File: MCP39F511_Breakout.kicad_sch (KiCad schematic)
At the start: 27 parts, among them J1 Conn_01x10, U1 MCP39F511-E_MQ, U2 MCP9700T-ETT, Y1 4MHz / 16pF

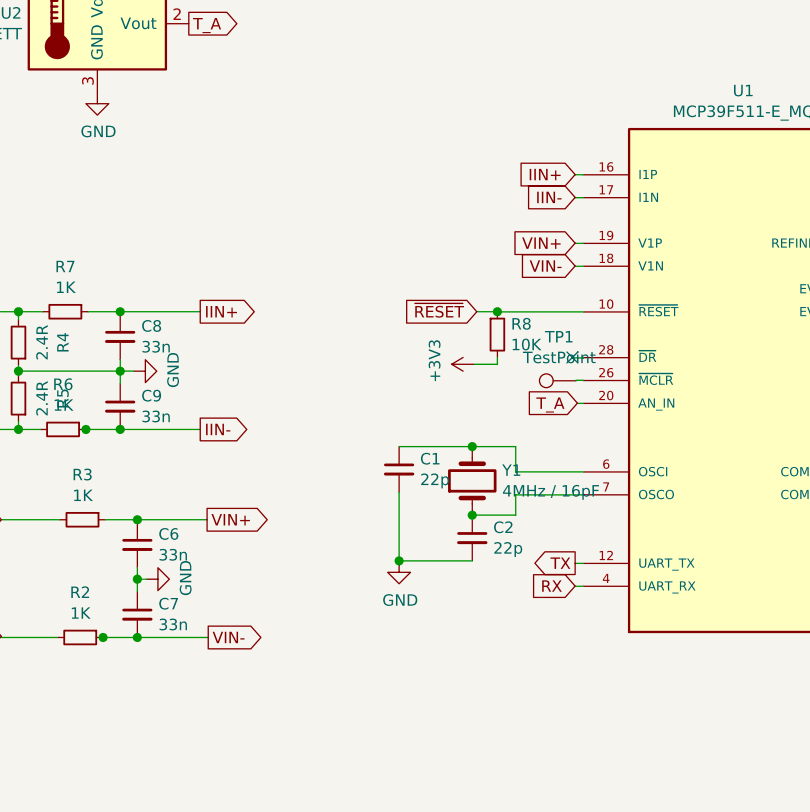
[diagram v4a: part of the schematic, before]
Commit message: Add MCLR pullup
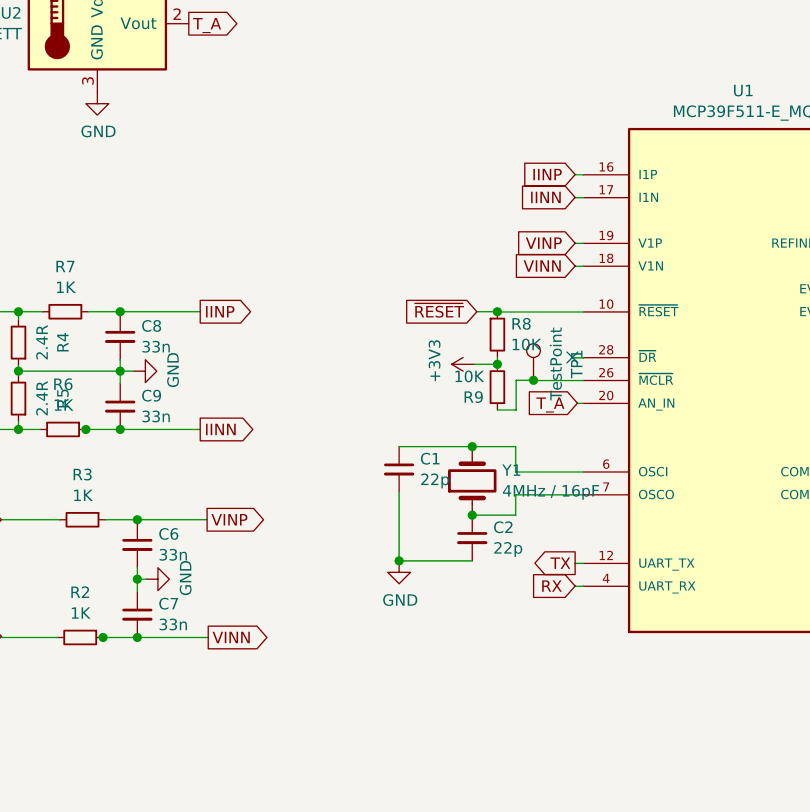
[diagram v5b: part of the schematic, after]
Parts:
- added R9: 10K, Resistor_SMD:R_0603_1608Metric, symbol Device:R_Small
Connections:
- net +3V3: now also R9.2
- net at TP1.1, U1.26 (~MCLR): now also R9.1
- net IIN+ renamed IINP
- net IIN- renamed IINN
- net VIN+ renamed VINP
- net VIN- renamed VINN
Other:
- moved on the sheet: TP1
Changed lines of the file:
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@@
   (junction (at 103.886 98.044) (diameter 1.016) (color 0 0 0 0))
   (junction (at 106.68 75.438) (diameter 1.016) (color 0 0 0 0))
+  (junction (at 106.68 81.28) (diameter 1.016) (color 0 0 0 0))
+  (junction (at 110.6932 83.058) (diameter 1.016) (color 0 0 0 0))
   (junction (at 151.7904 105.9434) (diameter 1.016) (color 0 0 0 0))
   (junction (at 151.7904 108.458) (diameter 1.016) (color 0 0 0 0))
@@
     (stroke (width 0) (type solid) (color 0 0 0 0))
   )
+  (wire (pts (xy 108.7628 83.058) (xy 108.7628 86.36))
+    (stroke (width 0) (type solid) (color 0 0 0 0))
+  )
+  (wire (pts (xy 108.7628 86.36) (xy 106.68 86.36))
+    (stroke (width 0) (type solid) (color 0 0 0 0))
+  )
+  (wire (pts (xy 110.6932 83.058) (xy 108.7628 83.058))
+    (stroke (width 0) (type solid) (color 0 0 0 0))
+  )
+  (wire (pts (xy 110.6932 83.0834) (xy 110.6932 83.058))
+    (stroke (width 0) (type solid) (color 0 0 0 0))
+  )
   (wire (pts (xy 115.0112 80.518) (xy 115.0112 80.5688))
     (stroke (width 0) (type solid) (color 0 0 0 0))
@@
     (stroke (width 0) (type solid) (color 0 0 0 0))
   )
-  (wire (pts (xy 115.4176 83.058) (xy 115.4176 83.1088))
-    (stroke (width 0) (type solid) (color 0 0 0 0))
-  )
   (wire (pts (xy 115.57 85.6234) (xy 115.57 85.598))
     (stroke (width 0) (type solid) (color 0 0 0 0))
@@
     (stroke (width 0) (type solid) (color 0 0 0 0))
   )
-  (wire (pts (xy 116.2304 83.058) (xy 115.4176 83.058))
-    (stroke (width 0) (type solid) (color 0 0 0 0))
-  )
-  (wire (pts (xy 116.2304 83.058) (xy 116.2304 83.0834))
+  (wire (pts (xy 116.2304 83.0834) (xy 110.6932 83.0834))
     (stroke (width 0) (type solid) (color 0 0 0 0))
   )
@@
     (effects (font (size 1.27 1.27)) (justify left))
   )
-  (global_label "IIN+" (shape output) (at 73.66 75.438 0)
+  (global_label "IINP" (shape output) (at 73.66 75.438 0)
     (effects (font (size 1.27 1.27)) (justify left))
   )
-  (global_label "IIN-" (shape output) (at 73.66 88.519 0)
+  (global_label "IINN" (shape output) (at 73.66 88.519 0)
     (effects (font (size 1.27 1.27)) (justify left))
   )
-  (global_label "VIN+" (shape output) (at 74.422 98.552 0)
+  (global_label "VINP" (shape output) (at 74.422 98.552 0)
     (effects (font (size 1.27 1.27)) (justify left))
   )
-  (global_label "VIN-" (shape output) (at 74.549 111.633 0)
+  (global_label "VINN" (shape output) (at 74.549 111.633 0)
     (effects (font (size 1.27 1.27)) (justify left))
   )
@@
     (effects (font (size 1.27 1.27)) (justify right))
   )
-  (global_label "IIN+" (shape input) (at 115.316 60.198 180)
+  (global_label "IINP" (shape input) (at 115.316 60.198 180)
     (effects (font (size 1.27 1.27)) (justify right))
   )
-  (global_label "IIN-" (shape input) (at 115.316 62.738 180)
+  (global_label "IINN" (shape input) (at 115.316 62.738 180)
     (effects (font (size 1.27 1.27)) (justify right))
   )
-  (global_label "VIN+" (shape input) (at 115.316 67.818 180)
+  (global_label "VINP" (shape input) (at 115.316 67.818 180)
     (effects (font (size 1.27 1.27)) (justify right))
   )
-  (global_label "VIN-" (shape input) (at 115.316 70.358 180)
+  (global_label "VINN" (shape input) (at 115.316 70.358 180)
     (effects (font (size 1.27 1.27)) (justify right))
   )
@@
     (effects (font (size 1.27 1.27)) (justify right))
   )
-  (symbol (lib_id "Connector:TestPoint") (at 115.4176 83.1088 90) (unit 1)
-    (in_bom yes) (on_board yes)
-    (property "Reference" "TP1" (id 0) (at 113.5761 78.2636 90))
-    (property "Value" "TestPoint" (id 1) (at 113.5761 80.5623 90))
-    (property "Footprint" "TestPoint:TestPoint_Pad_D2.0mm" (id 2) (at 115.4176 78.0288 0)
-      (effects (font (size 1.27 1.27)) hide)
-    )
-    (property "Datasheet" "~" (id 3) (at 115.4176 78.0288 0)
-      (effects (font (size 1.27 1.27)) hide)
-    )
-    (property "DNP" "..." (id 4) (at 115.4176 83.1088 0)
+  (symbol (lib_id "Connector:TestPoint") (at 110.6932 83.058 0) (unit 1)
+    (in_bom yes) (on_board yes)
+    (property "Reference" "TP1" (id 0) (at 115.5384 81.2165 90))
+    (property "Value" "TestPoint" (id 1) (at 113.2397 81.2165 90))
+    (property "Footprint" "TestPoint:TestPoint_Pad_D2.0mm" (id 2) (at 115.7732 83.058 0)
+      (effects (font (size 1.27 1.27)) hide)
+    )
+    (property "Datasheet" "~" (id 3) (at 115.7732 83.058 0)
+      (effects (font (size 1.27 1.27)) hide)
+    )
+    (property "DNP" "..." (id 4) (at 110.6932 83.058 0)
       (effects (font (size 1.27 1.27)) hide)
     )
@@
     )
     (property "manf#" "RC0603FR-0710KL" (id 4) (at 106.68 77.978 0)
+      (effects (font (size 1.27 1.27)) hide)
+    )
+  )
+  (symbol (lib_id "Device:R_Small") (at 106.68 83.82 180) (unit 1)
+    (in_bom yes) (on_board yes)
+    (property "Reference" "R9" (id 0) (at 105.1813 84.9694 0)
+      (effects (font (size 1.27 1.27)) (justify left))
+    )
+    (property "Value" "10K" (id 1) (at 105.1813 82.6707 0)
+      (effects (font (size 1.27 1.27)) (justify left))
+    )
+    (property "Footprint" "Resistor_SMD:R_0603_1608Metric" (id 2) (at 106.68 83.82 0)
+      (effects (font (size 1.27 1.27)) hide)
+    )
+    (property "Datasheet" "~" (id 3) (at 106.68 83.82 0)
+      (effects (font (size 1.27 1.27)) hide)
+    )
+    (property "manf#" "RC0603FR-0710KL" (id 4) (at 106.68 83.82 0)
       (effects (font (size 1.27 1.27)) hide)
     )
@@
       (reference "R8") (unit 1) (value "10K") (footprint "Resistor_SMD:R_0603_1608Metric")
     )
+    (path "/81d999fc-596b-402f-991d-76c616dcb90b"
+      (reference "R9") (unit 1) (value "10K") (footprint "Resistor_SMD:R_0603_1608Metric")
+    )
     (path "/12887168-a49a-4745-9d00-7dfb93b5e52d"

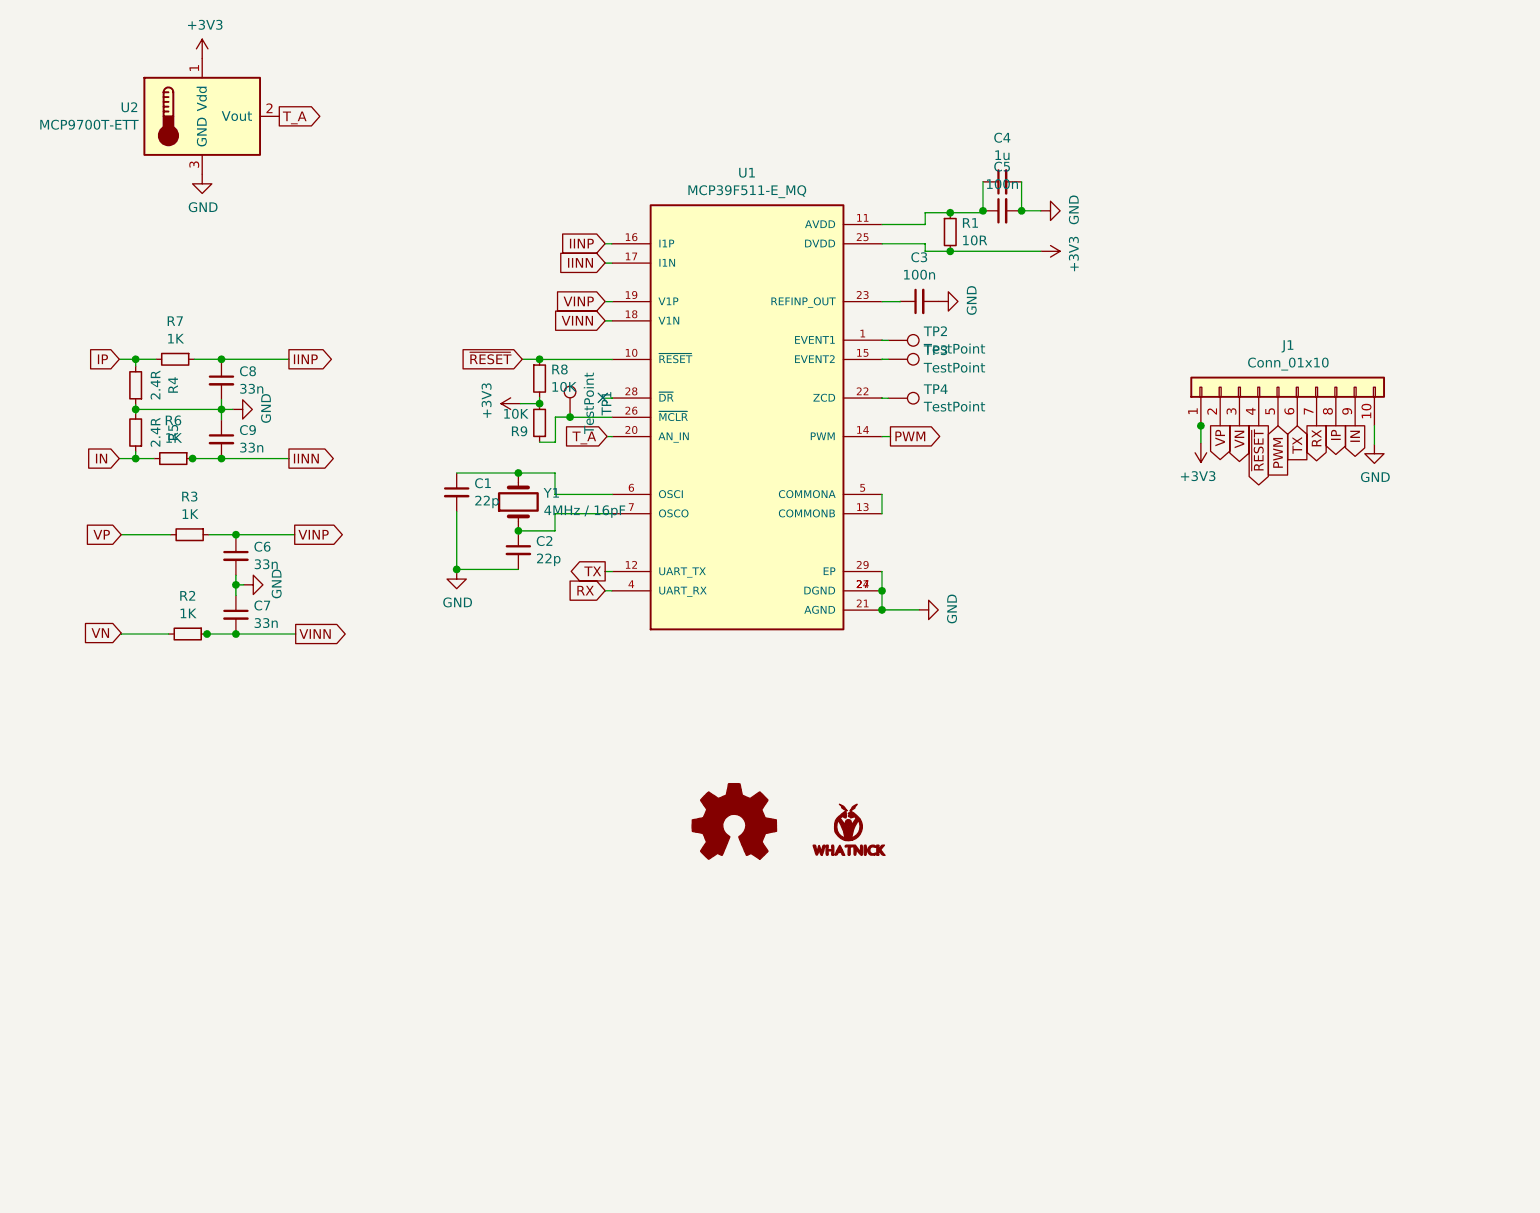
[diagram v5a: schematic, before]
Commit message: Schematic Cleanup, Notes added, PCB cleanup
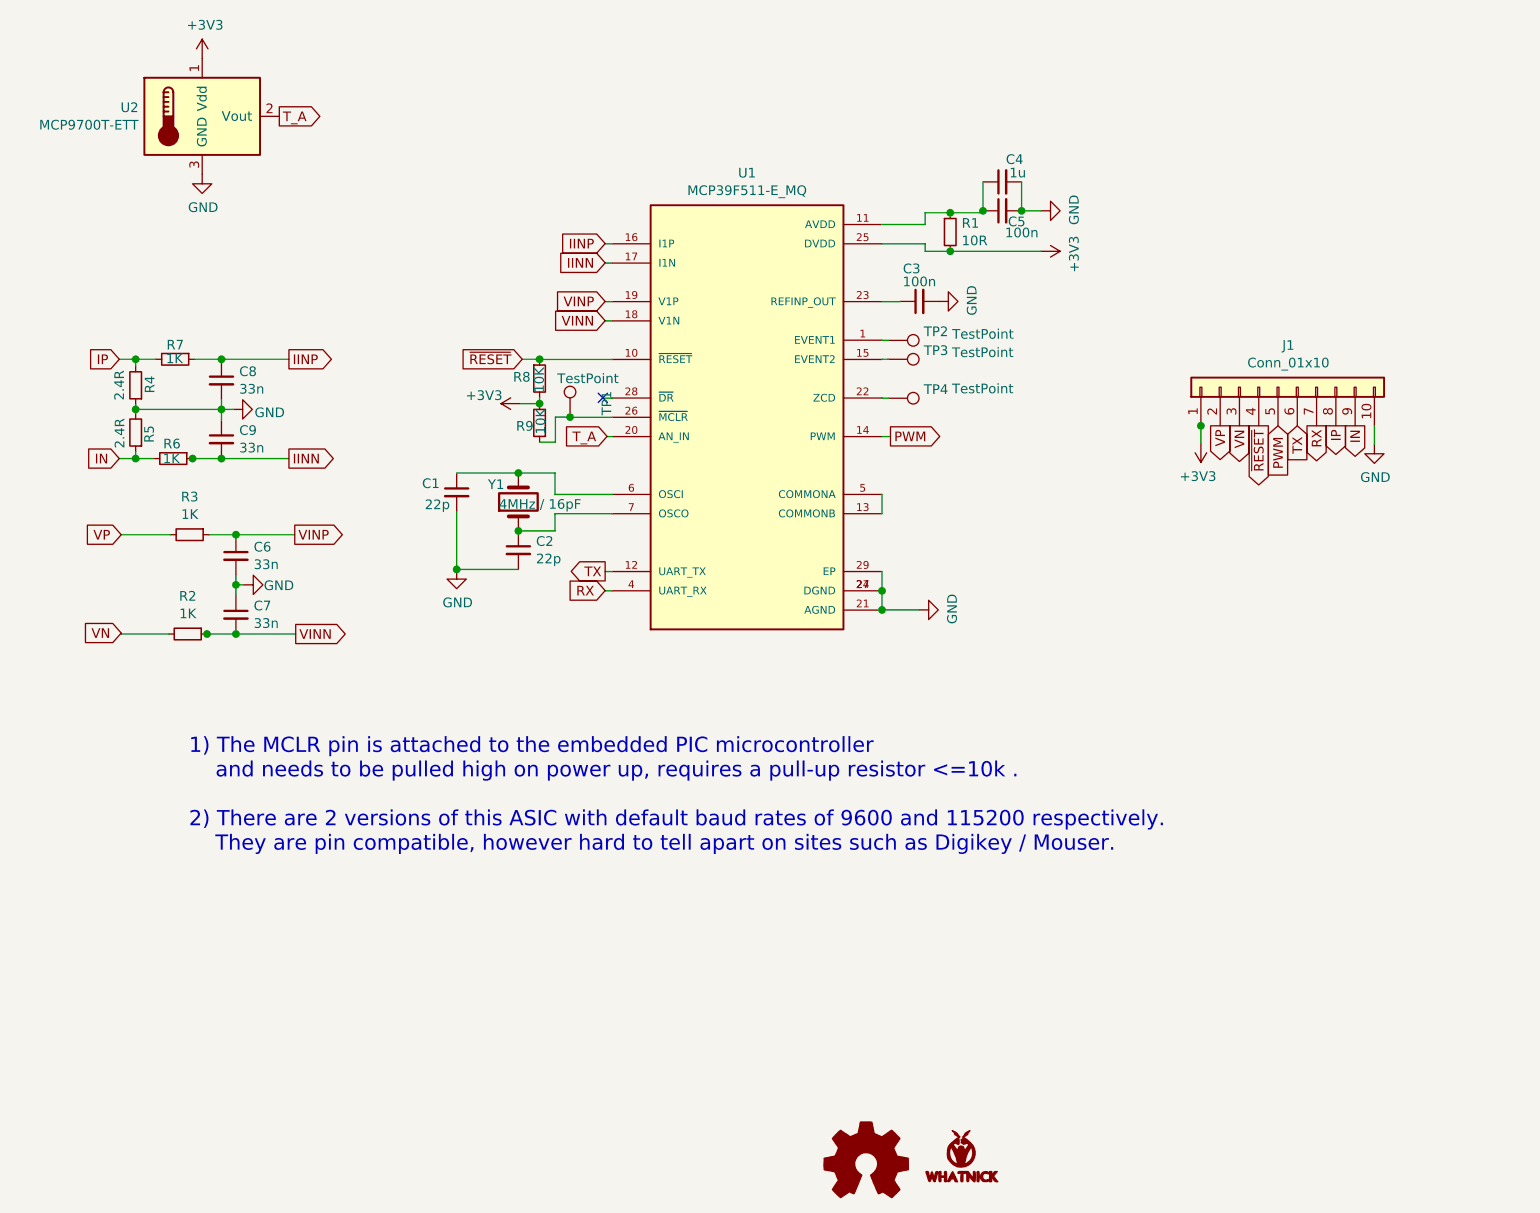
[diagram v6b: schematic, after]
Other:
- note added: "1) The MCLR pin is attached to the embedded PIC microcontroller and needs to be pulled high on power up, requires a pull-up resistor <=10k . 2) There are 2 versions of this ASIC with default baud rates of 9600 and 115200 respectively. They are pin compatible, however hard to tell apart on sites such as Digikey / Mouser."
